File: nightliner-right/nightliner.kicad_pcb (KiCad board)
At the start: 2 copper layers, 154.8 x 116.1 mm, 83 parts, among them J1 TYPE-C-31-M-12, J2 Battery, J3 Serial, P1 ISP_Prog, SW1 pinky_top, SW10 inner_home, SW11 pinky_bottom, SW12 ring_bottom, SW13 middle_bottom, SW14 index_bottom, SW15 inner_bottom, SW16 outer_top, SW17 outer_home, SW18 near_thumb, SW19 home_thumb, SW2 ring_top, SW20 far_thumb, SW21 ON_OFF, SW22 RESET, SW3 middle_top, SW4 index_top, SW5 inner_top, SW6 pinky_home, SW7 ring_home, SW8 middle_home, SW9 index_home, U1 holyiot-18010, U2 TVS2200DRV, U3 USBLC6-2SC6, U4 BQ24075RGT, U5 XC6220B331MR

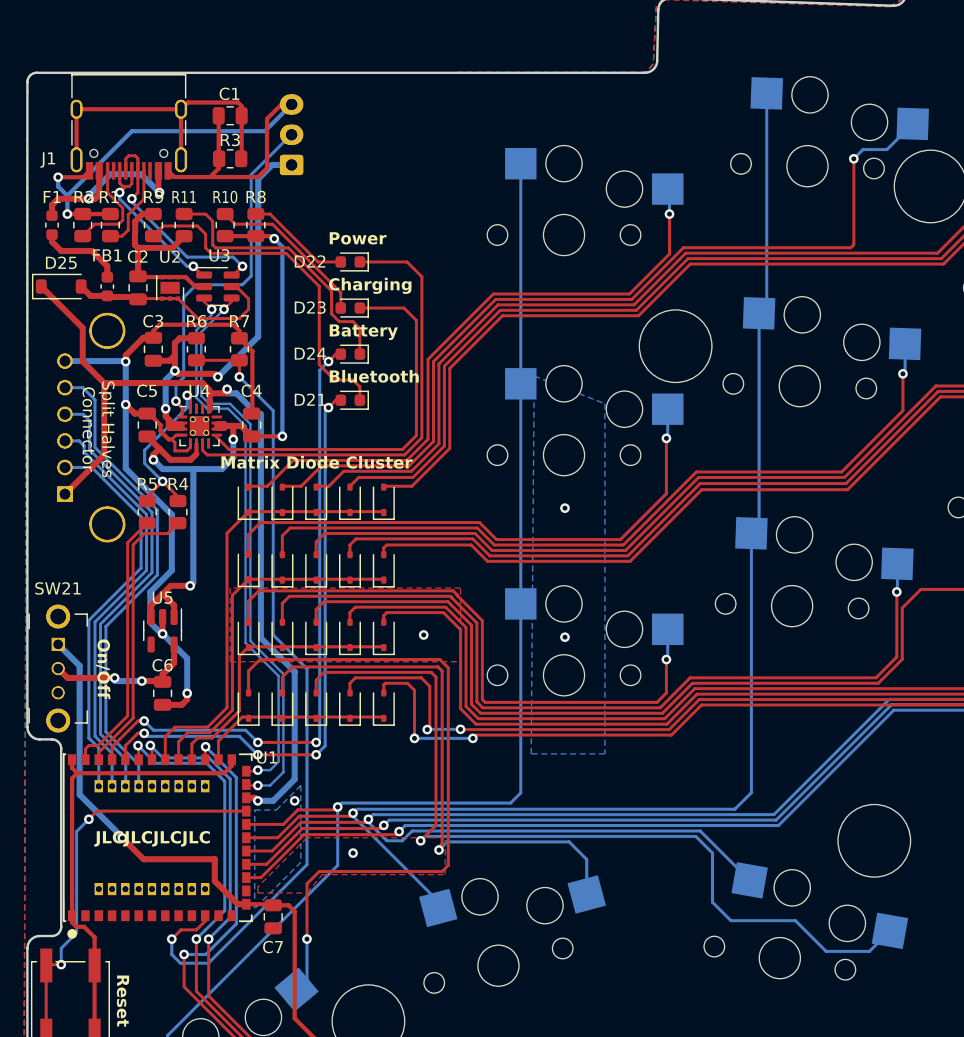
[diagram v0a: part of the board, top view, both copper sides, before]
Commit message: fix: make sides symmetric
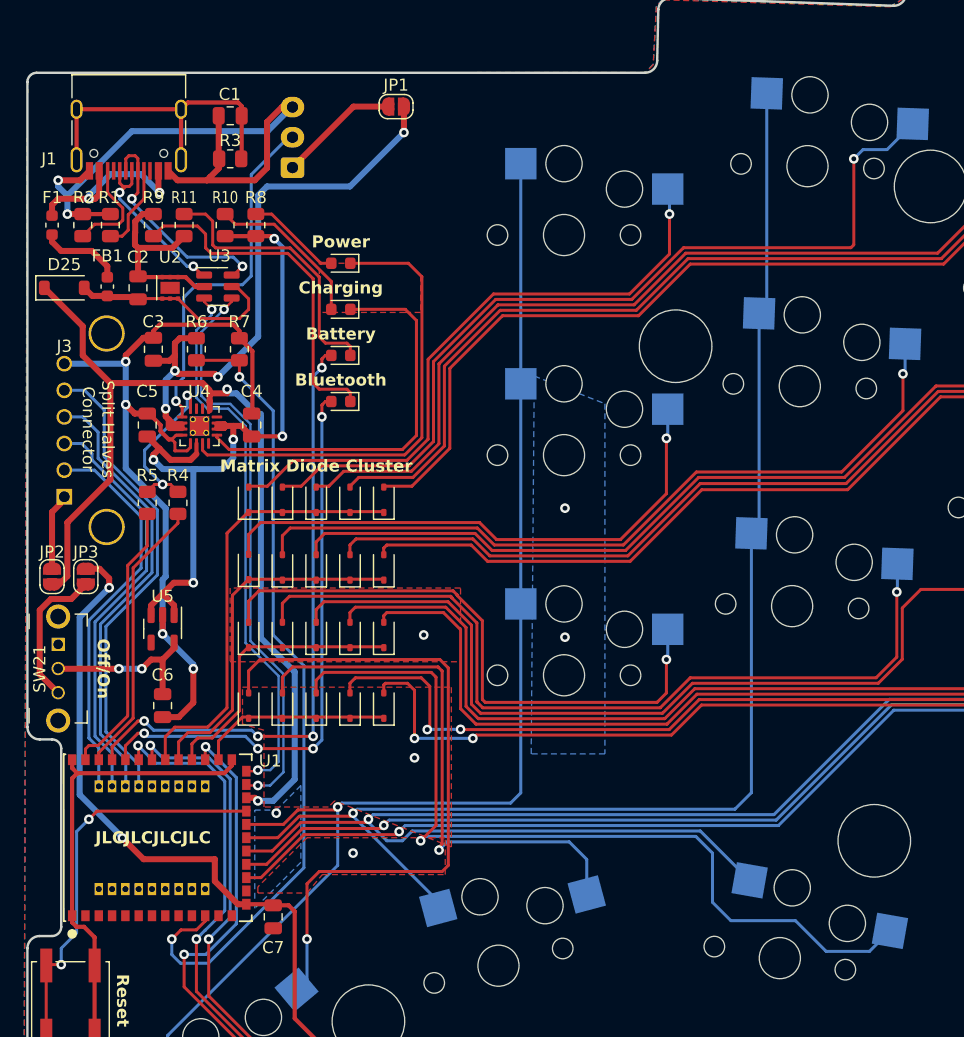
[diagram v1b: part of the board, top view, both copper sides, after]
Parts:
- added JP1: VBAT, Jumper:SolderJumper-2_P1.3mm_Open_RoundedPad1.0x1.5mm, F.Cu at (66.0, 40.9)
- added JP2: VBUS, Jumper:SolderJumper-2_P1.3mm_Open_RoundedPad1.0x1.5mm, F.Cu at (37.6, 79.8)
- added JP3: VDD, Jumper:SolderJumper-2_P1.3mm_Open_RoundedPad1.0x1.5mm, F.Cu at (40.4, 79.8)
- moved C6 1.02 mm to (46.7, 90.4)
- moved D21 0.79 mm to (61.5, 65.3)
- moved D22 0.79 mm to (61.5, 53.8)
- moved D23 0.79 mm to (61.5, 57.7)
- moved D24 0.79 mm to (61.5, 61.5)
- moved R4 0.76 mm to (48.0, 73.7)
- moved R5 0.76 mm to (45.5, 73.7)
- moved D25 0.28 mm to (38.6, 55.9)
- moved J2 0.23 mm to (57.5, 45.9)
- moved J3 0.22 mm to (38.6, 73.2)
- moved U5 0.16 mm to (46.7, 84.1)
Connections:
- J2 pad 1: /VBAT -> Net-(JP1-B)
- J3 pad 1: VBUS -> Net-(J3-Pin_1)
- SW21 pad 1: VDD -> unconnected-(SW21-A-Pad1)
- SW21 pad 3: unconnected-(SW21-C-Pad3) -> Net-(JP3-A)
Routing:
- net Net-(JP3-A): track 0.00 -> 12.1 mm
- net /VBAT: track 38.1 -> 49.8 mm, vias 3 -> 4
- net Net-(JP1-B): track 0.00 -> 10.0 mm
- net VDD: track 57.8 -> 65.8 mm, vias 2 -> 3
- net VBUS: track 72.4 -> 80.3 mm
- net Net-(J3-Pin_1): track 0.00 -> 6.37 mm
- net BT_LED: track 48.5 -> 47.2 mm
- net BAT_STAT: track 52.7 -> 51.5 mm
- net Net-(U4-ISET): track 14.7 -> 13.7 mm
- net Net-(SW21-B): track 12.5 -> 13.5 mm
- net CHARGE_CTRL_2: track 22.1 -> 22.9 mm
- net Net-(D22-K): track 38.4 -> 39.1 mm
- net Net-(D23-K): track 32.2 -> 32.9 mm
- net Net-(D22-A): track 8.66 -> 7.92 mm
- net GND: track 197.2 -> 197.5 mm, vias 12 -> 13
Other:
- board text added: "Off/On"
- board text added: "v1.0"
- board text removed: "On/Off"

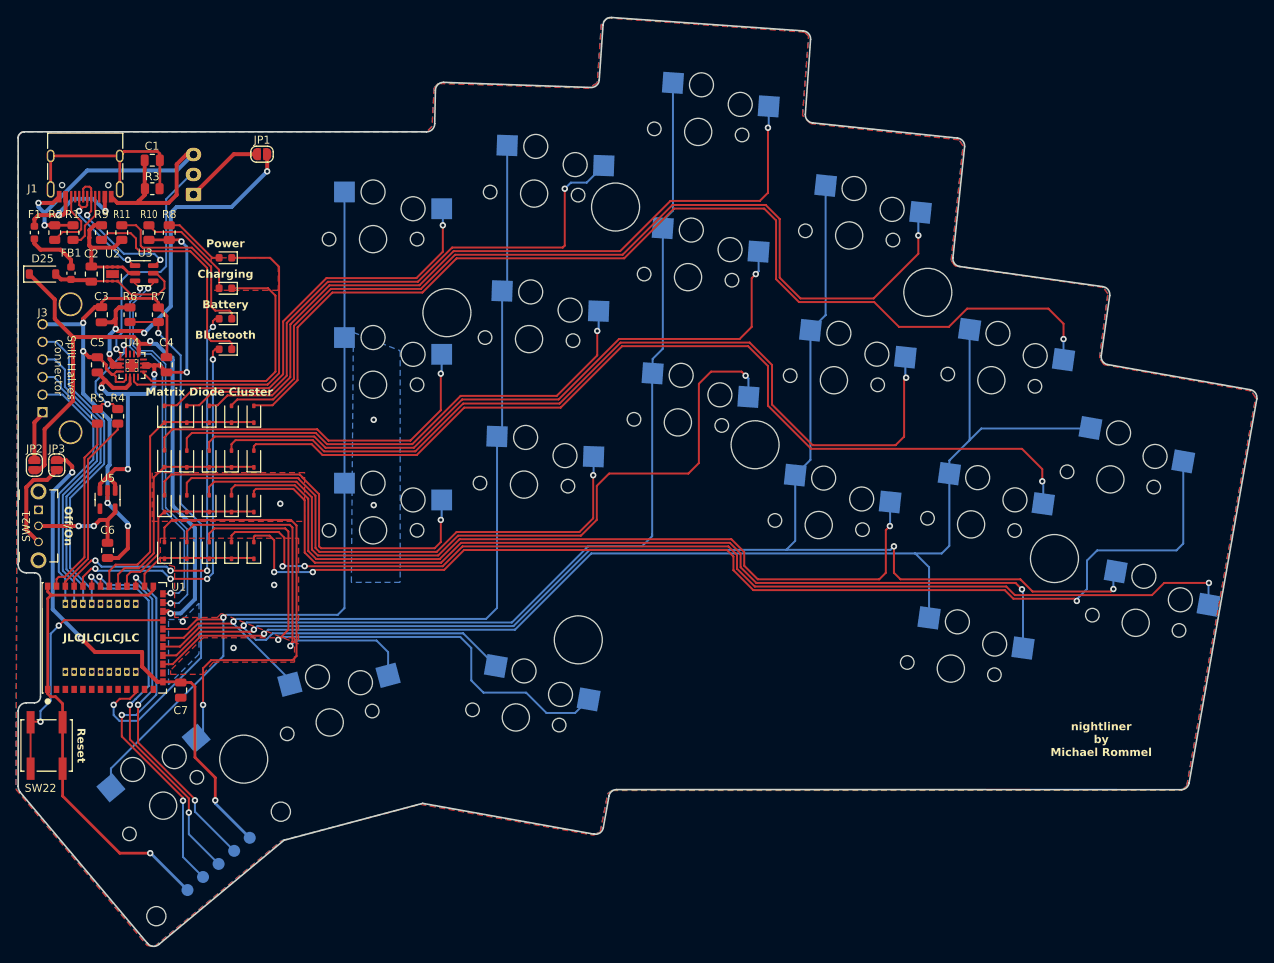
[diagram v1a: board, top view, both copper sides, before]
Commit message: feat: initial right side case completed
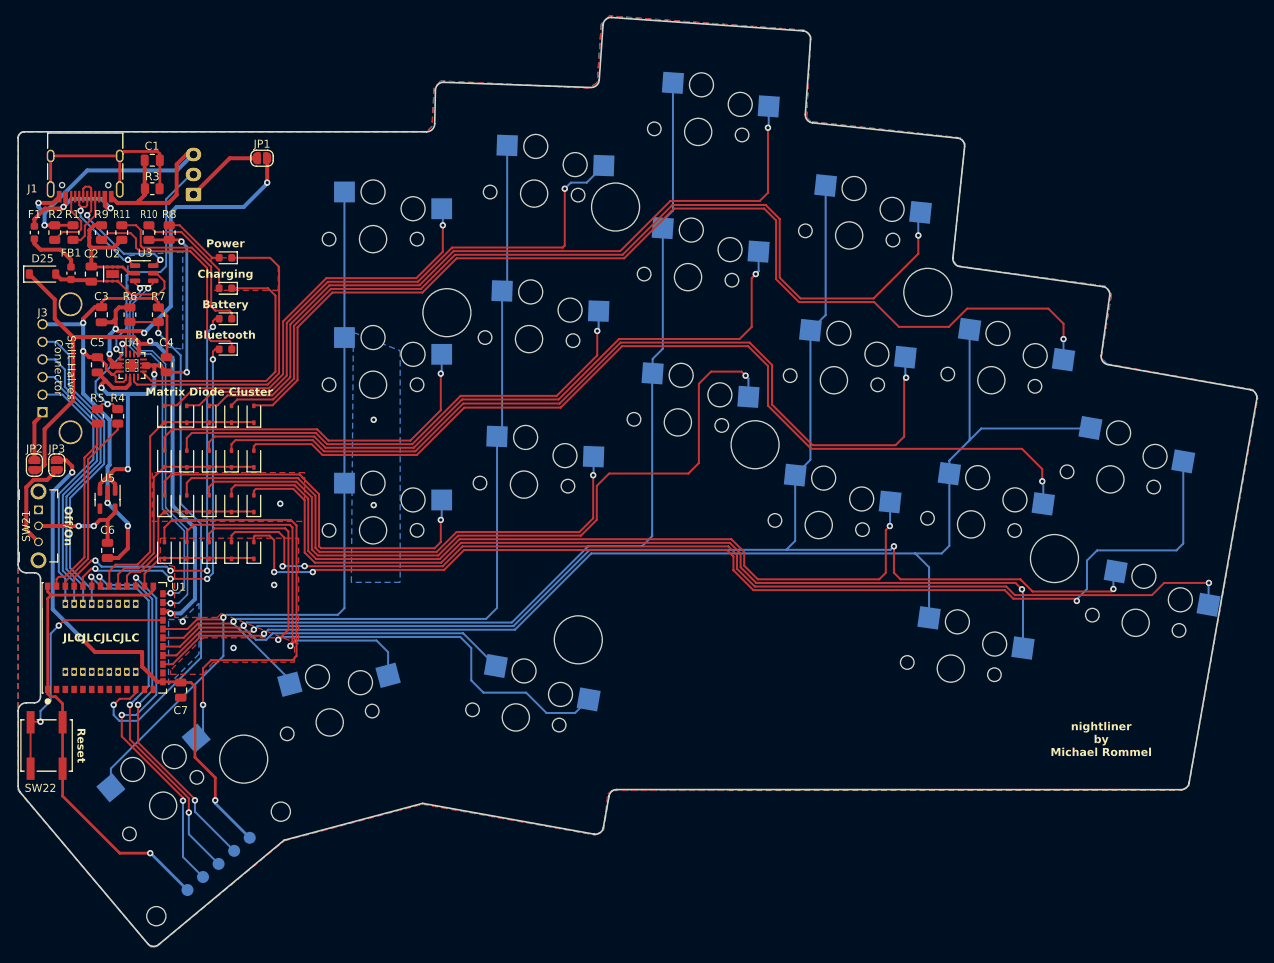
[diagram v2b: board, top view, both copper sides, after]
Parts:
- P1: value ISP_Prog -> ISP
- moved JP1 0.51 mm to (66.0, 41.4)
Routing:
- net Net-(F1-Pad1): track 16.4 -> 15.3 mm

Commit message: fix: change edge outline, flip switches
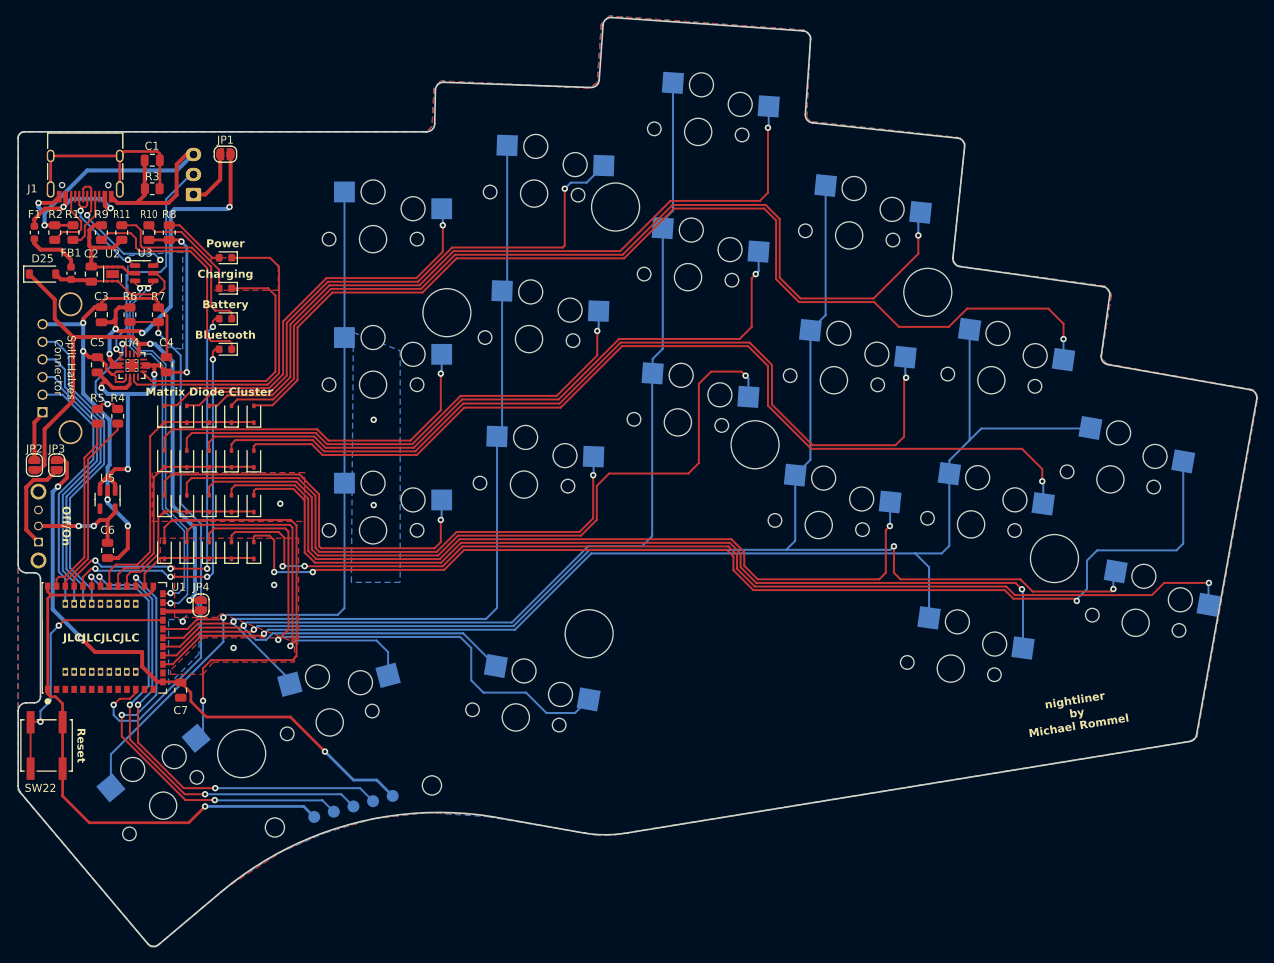
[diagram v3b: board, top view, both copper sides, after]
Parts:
- added JP4: VBUS, Jumper:SolderJumper-2_P1.3mm_Open_RoundedPad1.0x1.5mm, F.Cu at (58.4, 97.3)
- P1: value ISP -> ISP_Prog
- SW21: moved to B.Cu
- moved P1 19.2 mm to (87.3, 119.8), turned to -165 degrees
- moved JP1 4.60 mm to (61.5, 40.9)
- moved SW21 4.02 mm to (38.1, 89.4), turned to 90 degrees
- moved H6 1.55 mm to (106.9, 100.8)
- moved H7 0.74 mm to (63.5, 115.8)
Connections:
- SW21 pad 1: unconnected-(SW21-A-Pad1) -> Net-(JP3-A)
- SW21 pad 3: Net-(JP3-A) -> unconnected-(SW21-C-Pad3)
- U1 pad 47: VBUS -> Net-(JP4-B)
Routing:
- net SWCLK: track 46.2 -> 60.1 mm
- net GND: track 197.5 -> 210.8 mm
- net SWDIO: track 48.3 -> 59.6 mm
- net SWO: track 46.6 -> 55.2 mm
- net VDD: track 65.8 -> 74.4 mm
- net Net-(JP4-B): track 0.00 -> 5.17 mm
- net VBUS: track 80.3 -> 76.9 mm
- net Net-(JP1-B): track 9.79 -> 7.30 mm
- net /VBAT: track 50.2 -> 47.8 mm
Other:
- outline, holes or cut-outs redrawn

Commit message: feat: outline change, fix right pinky column
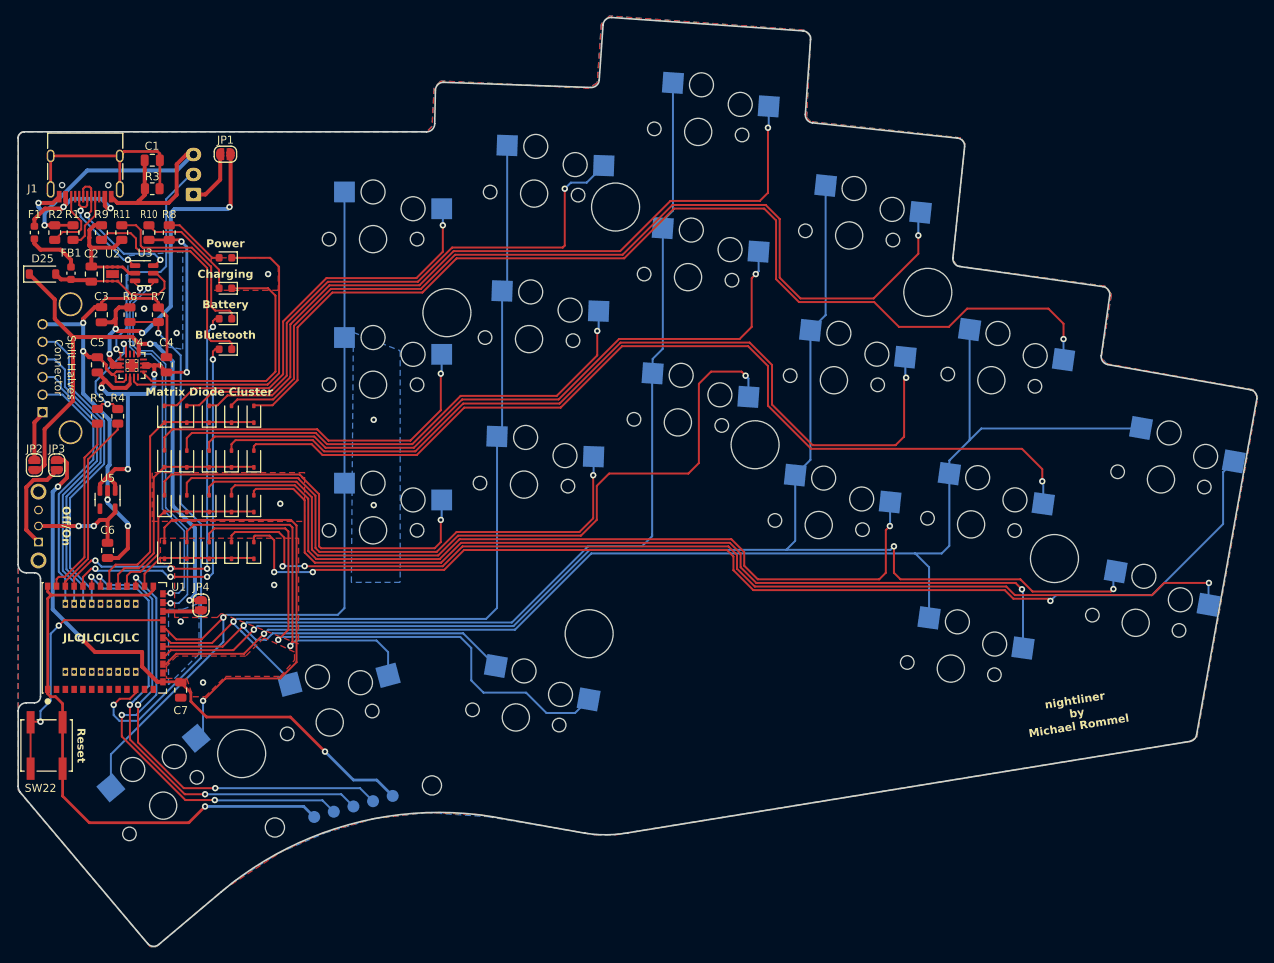
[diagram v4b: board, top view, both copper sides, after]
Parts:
- moved SW16 6.32 mm to (178.4, 81.5)
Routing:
- net COL0: track 158.2 -> 164.5 mm
- net Net-(D20-A): track 56.7 -> 54.7 mm
- net Net-(D16-A): track 141.3 -> 143.2 mm
- net COL4: track 103.2 -> 104.2 mm
- net COL3: track 112.4 -> 113.0 mm
- net GND: vias 13 -> 16
